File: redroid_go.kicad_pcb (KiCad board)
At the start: 2 copper layers, 70 x 95 mm, 98 parts, among them J1 USB4105-GF-A, J2 5051101892, J3 Conn_01x02_Pin, J4 Conn_01x10_Pin, Q1 UMH3N, Q2 PMOS, Q3 UMH3N, SW1 UP, SW10 A, SW11 SW_SPDT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

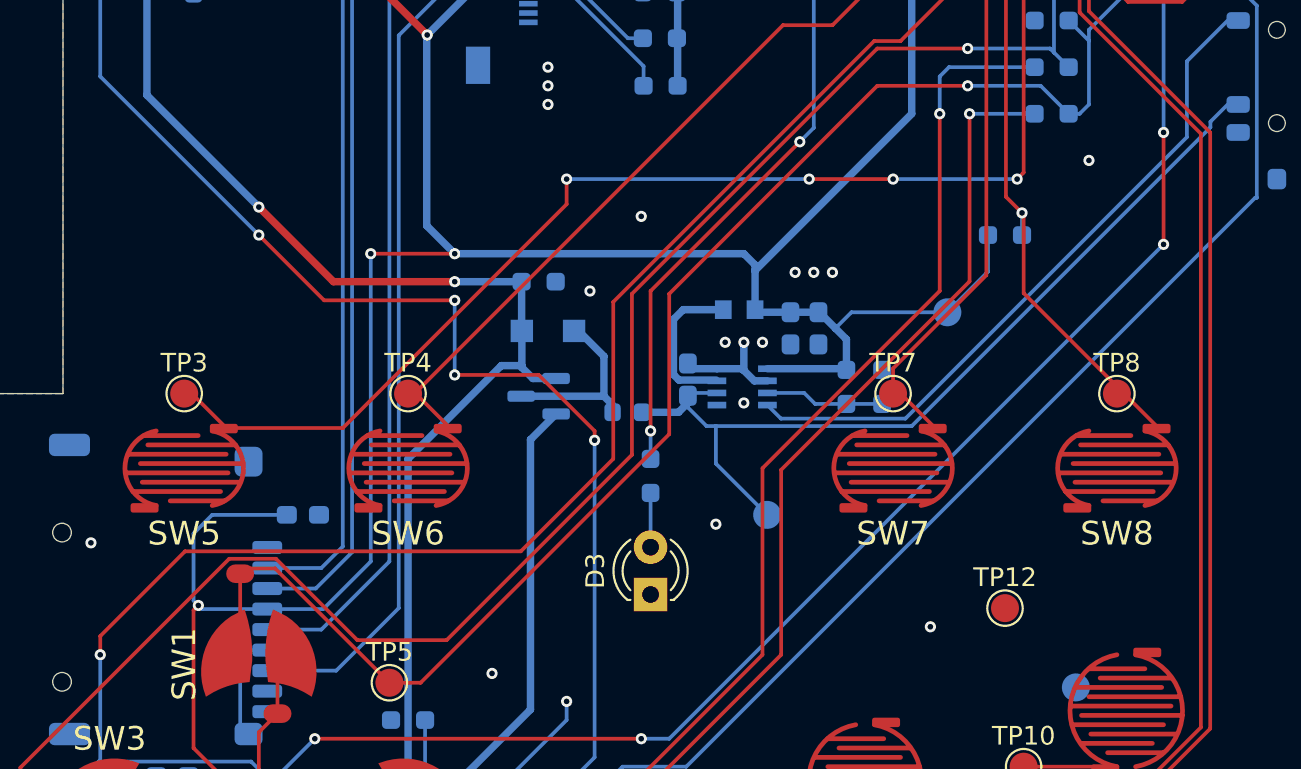
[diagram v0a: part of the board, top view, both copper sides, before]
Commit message: Update menu button footprints
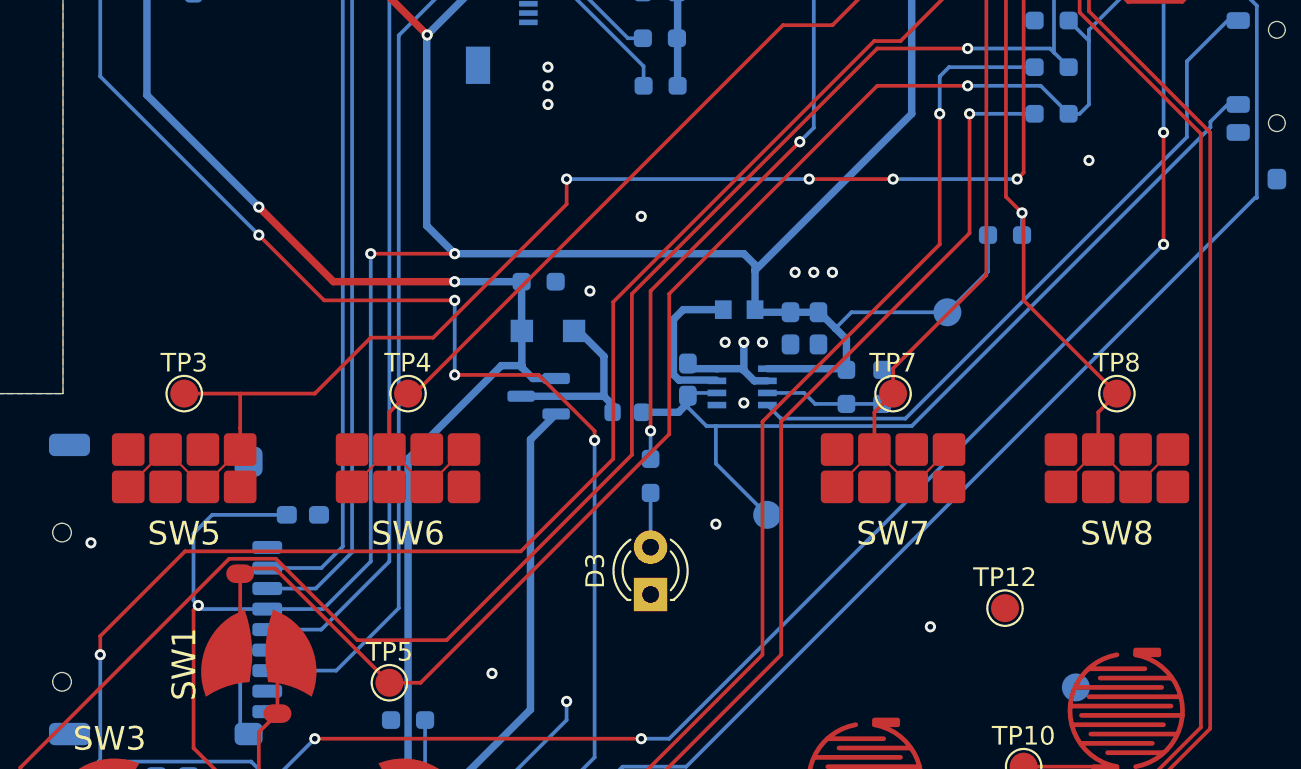
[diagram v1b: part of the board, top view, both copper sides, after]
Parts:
- SW5, SW6, SW7, SW8: footprint Conductive Button:CONDUCTIVE_BUTTON_STARTSELECT -> Conductive Button:CONDUCTIVE_BUTTON_THICK_STARTSELECT
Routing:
- net IO13: track 78.5 -> 79.8 mm
- net IO0: track 71.4 -> 72.2 mm
- net IO27: track 47.5 -> 48.3 mm
- net IO39: track 55.0 -> 55.6 mm

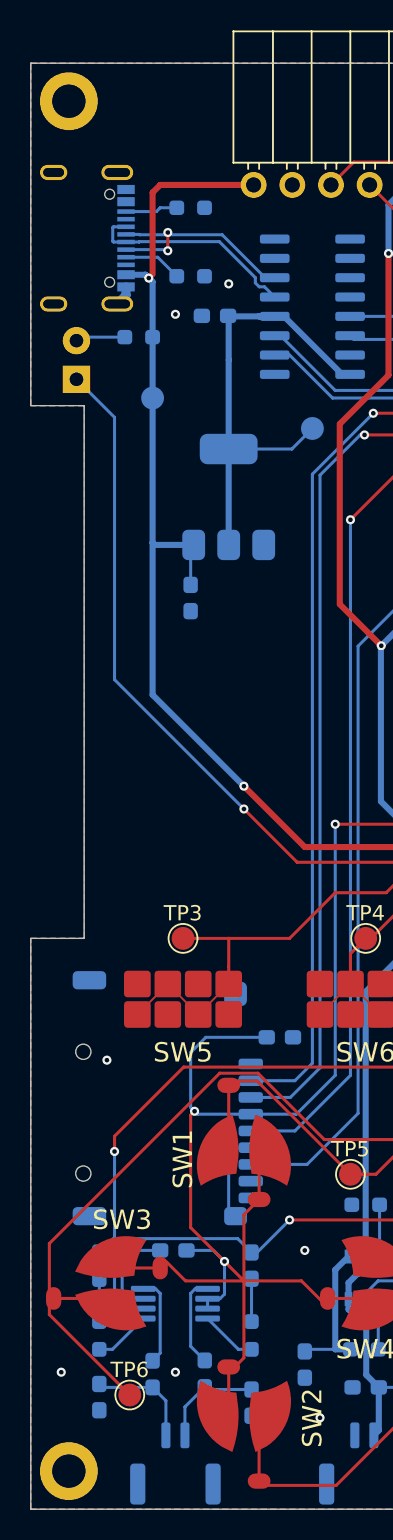
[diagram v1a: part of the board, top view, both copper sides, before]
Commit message: Fix board display margin
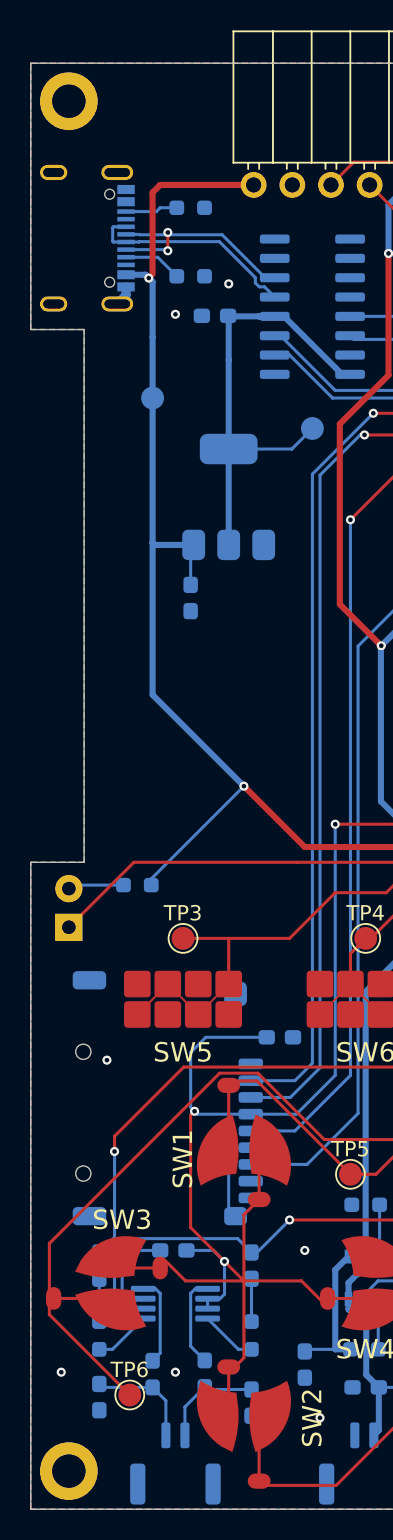
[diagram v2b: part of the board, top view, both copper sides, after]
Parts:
- moved D2 36.0 mm to (131.0, 100.3)
- moved R8 36.0 mm to (135.5, 97.5)
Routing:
- net Net-(D2-K): track 89.3 -> 68.3 mm, vias 4 -> 3
- net VBUS: track 113.9 -> 122.9 mm
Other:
- outline, holes or cut-outs redrawn
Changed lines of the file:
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@@
 	(footprint "Resistor_SMD:R_0603_1608Metric_Pad0.98x0.95mm_HandSolder"
 		(layer "B.Cu")
-		(at 135.5875 61.5 180)
+		(at 135.5 97.5 180)
 		(descr "Resistor SMD 0603 (1608 Metric), square (rectangular) end terminal, IPC_7351 nominal with elongated pad for handsoldering. (Body size source: IPC-SM-782 page 72, https://www.pcb-3d.com/wordpress/wp-content/uploads/ipc-sm-782a_amendment_1_and_2.pdf), generated with kicad-footprint-generator")
 		(tags "resistor handsolder")
@@
 	(footprint "LED_THT:LED_D3.0mm"
 		(layer "B.Cu")
-		(at 131.5 64.27 90)
+		(at 131 100.27 90)
 		(descr "LED, diameter 3.0mm, 2 pins, generated by kicad-footprint-generator")
 		(tags "LED")
@@
 	)
 	(gr_line
-		(start 128.5 101)
-		(end 132 101)
+		(start 128.5 96)
+		(end 132 96)
 		(stroke
 			(width 0.05)
@@
 	)
 	(gr_line
-		(start 128.5 66)
-		(end 132 66)
+		(start 128.5 61)
+		(end 132 61)
 		(stroke
 			(width 0.05)
@@
 	)
 	(gr_line
-		(start 132 66)
-		(end 132 101)
+		(start 132 61)
+		(end 132 96)
 		(stroke
 			(width 0.05)
-			(type default)
+			(type solid)
 		)
 		(layer "Edge.Cuts")
@@
 	(gr_line
 		(start 128.5 43.5)
-		(end 128.5 66)
+		(end 128.5 61)
 		(stroke
 			(width 0.05)
@@
 	(gr_line
 		(start 128.5 138.5)
-		(end 128.5 101)
+		(end 128.5 96)
 		(stroke
 			(width 0.05)
@@
 	)
 	(segment
+		(start 136.4125 97.5)
+		(end 136.4125 97.0875)
+		(width 0.2)
+		(layer "B.Cu")
+		(net 5)
+	)
+	(segment
+		(start 136.4125 97.0875)
+		(end 142.5 91)
+		(width 0.2)
+		(layer "B.Cu")
+		(net 5)
+	)
+	(segment
 		(start 156.5875 95)
 		(end 153 95)
@@
 	)
 	(segment
-		(start 131.73 61.5)
-		(end 131.5 61.73)
+		(start 134.5875 97.5)
+		(end 131.23 97.5)
 		(width 0.2)
 		(layer "B.Cu")
@@
 	)
 	(segment
-		(start 134.675 61.5)
-		(end 131.73 61.5)
+		(start 131.23 97.5)
+		(end 131 97.73)
 		(width 0.2)
 		(layer "B.Cu")
@@
 	)
 	(segment
-		(start 146 96)
-		(end 142.5 92.5)
+		(start 160.5 103)
+		(end 160.5 103.5)
 		(width 0.2)
 		(layer "F.Cu")
@@
 	)
 	(segment
-		(start 160.5 103)
-		(end 160.5 103.5)
+		(start 131 100.27)
+		(end 135.27 96)
 		(width 0.2)
 		(layer "F.Cu")
@@
 	)
 	(segment
+		(start 135.27 96)
+		(end 146 96)
+		(width 0.2)
+		(layer "F.Cu")
+		(net 16)
+	)
+	(segment
 		(start 153 96)
 		(end 146 96)
@@
 	)
 	(via
-		(at 142.5 92.5)
-		(size 0.6)
-		(drill 0.3)
-		(layers "F.Cu" "B.Cu")
-		(net 16)
-	)
-	(via
 		(at 153 100)
 		(size 0.6)
@@
 	)
 	(segment
-		(start 142.5 92.5)
-		(end 134 84)
-		(width 0.2)
-		(layer "B.Cu")
-		(net 16)
-	)
-	(segment
-		(start 134 66.77)
-		(end 131.5 64.27)
-		(width 0.2)
-		(layer "B.Cu")
-		(net 16)
-	)
-	(segment
 		(start 153 96)
 		(end 153 100)
@@
 	)
 	(segment
-		(start 134 84)
-		(end 134 66.77)
-		(width 0.2)
-		(layer "B.Cu")
-		(net 16)
-	)
-	(segment
 		(start 151.325 124.747629)
 		(end 151.273211 124.69584)
@@
 		(polygon
 			(pts
-				(xy 198.5 50) (xy 198.5 128.5) (xy 158.5 128.5) (xy 158.5 138.5) (xy 128.5 138.5) (xy 128.5 101)
-				(xy 132 101) (xy 132 66) (xy 128.5 66) (xy 128.5 43.5) (xy 173.5 43.5) (xy 173.5 50)
+				(xy 198.5 50) (xy 198.5 128.5) (xy 158.5 128.5) (xy 158.5 138.5) (xy 128.5 138.5) (xy 128.5 96)
+				(xy 132 96) (xy 132 61) (xy 128.5 61) (xy 128.5 43.5) (xy 173.5 43.5) (xy 173.5 50)
 			)
 		)
@@
 		(polygon
 			(pts
-				(xy 198.5 50) (xy 198.5 128.5) (xy 158.5 128.5) (xy 158.5 138.5) (xy 128.5 138.5) (xy 128.5 101)
-				(xy 132 101) (xy 132 66) (xy 128.5 66) (xy 128.5 43.5) (xy 173.5 43.5) (xy 173.5 50)
+				(xy 198.5 50) (xy 198.5 128.5) (xy 158.5 128.5) (xy 158.5 138.5) (xy 128.5 138.5) (xy 128.5 96)
+				(xy 132 96) (xy 132 61) (xy 128.5 61) (xy 128.5 43.5) (xy 173.5 43.5) (xy 173.5 50)
 			)
 		)

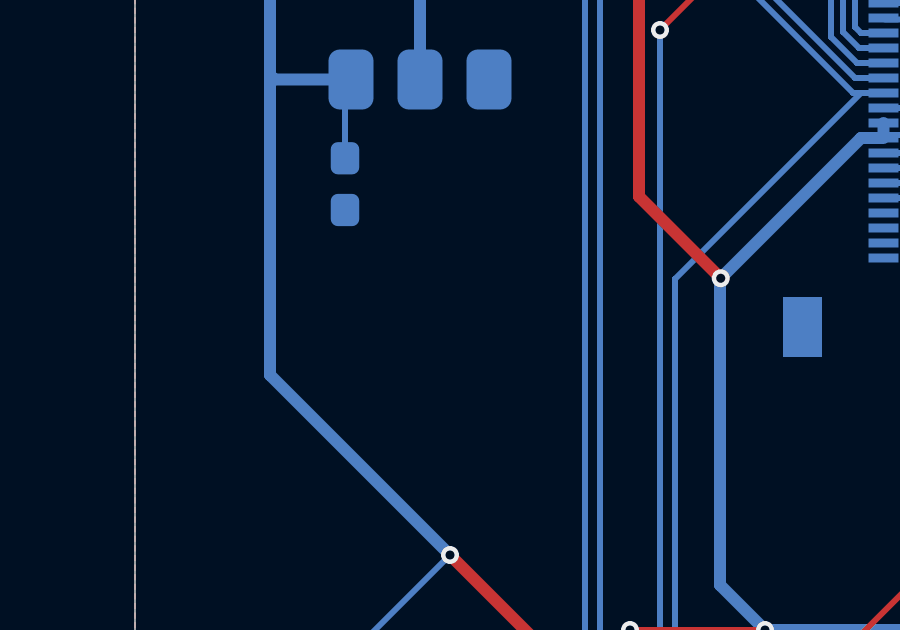
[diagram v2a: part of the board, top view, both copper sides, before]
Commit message: Add missing via
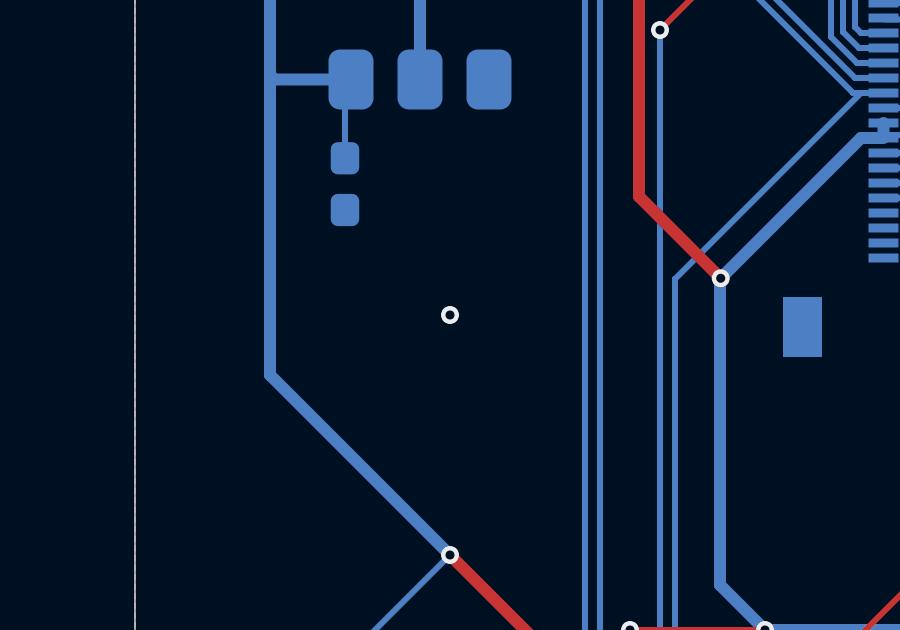
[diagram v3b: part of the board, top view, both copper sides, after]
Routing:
- net GND: vias 34 -> 35
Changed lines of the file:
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@@
+	)
+	(via
+		(at 142.5 83)
+		(size 0.6)
+		(drill 0.3)
+		(layers "F.Cu" "B.Cu")
+		(free yes)
+		(net 1)
 	)
 	(via

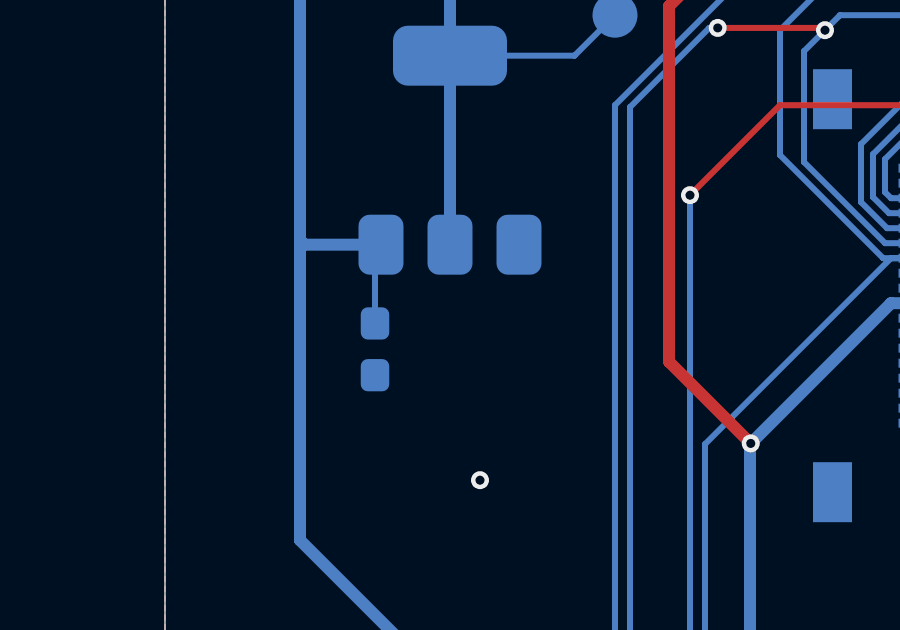
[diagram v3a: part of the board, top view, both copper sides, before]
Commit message: Fix 3V3_SERIAL capacitors
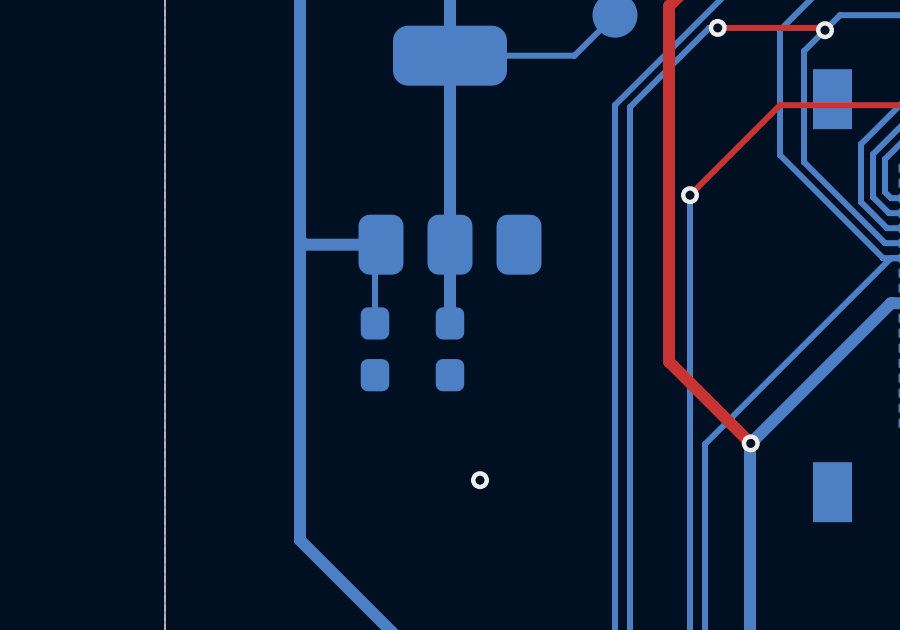
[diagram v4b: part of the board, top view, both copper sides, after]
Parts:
- added C18: 22uF, Capacitor_SMD:C_0603_1608Metric_Pad1.08x0.95mm_HandSolder, B.Cu at (141.5, 78.6)
- C14, C15: value 0.1uF -> 220pF
- C17: value 0.1uF -> 10uF
- R6: value 100k -> 2k
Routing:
- net P3V3_SERIAL: track 33.0 -> 35.6 mm
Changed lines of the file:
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@@
 			(layers "F.Cu" "F.Mask")
 			(roundrect_rratio 0.125)
-			(pinfunction "P$ACTIVE")
-			(pintype "bidirectional")
 			(solder_mask_margin 0.1016)
 			(solder_paste_margin 0)
@@
 			(layers "F.Cu" "F.Mask")
 			(roundrect_rratio 0.125)
-			(pinfunction "P$ACTIVE")
-			(pintype "bidirectional")
 			(solder_mask_margin 0.1016)
 			(solder_paste_margin 0)
@@
 			(layers "F.Cu" "F.Mask")
 			(roundrect_rratio 0.125)
-			(pinfunction "P$ACTIVE")
-			(pintype "bidirectional")
 			(solder_mask_margin 0.1016)
 			(solder_paste_margin 0)
@@
 			)
 		)
-		(property "Value" "0.1uF"
+		(property "Value" "10uF"
 			(at 0 -1.43 90)
 			(layer "B.Fab")
@@
 			)
 		)
-		(property "Value" "0.1uF"
+		(property "Value" "220pF"
 			(at 0 -1.43 90)
 			(layer "B.Fab")
@@
 		)
 	)
+	(footprint "Capacitor_SMD:C_0603_1608Metric_Pad1.08x0.95mm_HandSolder"
+		(layer "B.Cu")
+		(at 141.5 78.6375 -90)
+		(descr "Capacitor SMD 0603 (1608 Metric), square (rectangular) end terminal, IPC_7351 nominal with elongated pad for handsoldering. (Body size source: IPC-SM-782 page 76, https://www.pcb-3d.com/wordpress/wp-content/uploads/ipc-sm-782a_amendment_1_and_2.pdf), generated with kicad-footprint-generator")
+		(tags "capacitor handsolder")
+		(property "Reference" "C18"
+			(at 0 -2 90)
+			(layer "B.SilkS")
+			(effects
+				(font
+					(size 1 1)
+					(thickness 0.15)
+				)
+				(justify mirror)
+			)
+		)
+		(property "Value" "22uF"
+			(at 0 -1.43 90)
+			(layer "B.Fab")
+			(effects
+				(font
+					(size 1 1)
+					(thickness 0.15)
+				)
+				(justify mirror)
+			)
+		)
+		(property "Datasheet" ""
+			(at 0 0 90)
+			(unlocked yes)
+			(layer "B.Fab")
+			(hide yes)
+			(effects
+				(font
+					(size 1.27 1.27)
+					(thickness 0.15)
+				)
+				(justify mirror)
+			)
+		)
+		(property "Description" "Unpolarized capacitor"
+			(at 0 0 90)
+			(unlocked yes)
+			(layer "B.Fab")
+			(hide yes)
+			(effects
+				(font
+					(size 1.27 1.27)
+					(thickness 0.15)
+				)
+				(justify mirror)
+			)
+		)
+		(property ki_fp_filters "C_*")
+		(sheetname "/")
+		(sheetfile "redroid_go.kicad_sch")
+		(attr smd)
+		(fp_line
+			(start -0.146267 0.51)
+			(end 0.146267 0.51)
+			(stroke
+				(width 0.12)
+				(type solid)
+			)
+			(layer "B.SilkS")
+		)
+		(fp_line
+			(start -0.146267 -0.51)
+			(end 0.146267 -0.51)
+			(stroke
+				(width 0.12)
+				(type solid)
+			)
+			(layer "B.SilkS")
+		)
+		(fp_line
+			(start -1.65 0.73)
+			(end 1.65 0.73)
+			(stroke
+				(width 0.05)
+				(type solid)
+			)
+			(layer "B.CrtYd")
+		)
+		(fp_line
+			(start 1.65 0.73)
+			(end 1.65 -0.73)
+			(stroke
+				(width 0.05)
+				(type solid)
+			)
+			(layer "B.CrtYd")
+		)
+		(fp_line
+			(start -1.65 -0.73)
+			(end -1.65 0.73)
+			(stroke
+				(width 0.05)
+				(type solid)
+			)
+			(layer "B.CrtYd")
+		)
+		(fp_line
+			(start 1.65 -0.73)
+			(end -1.65 -0.73)
+			(stroke
+				(width 0.05)
+				(type solid)
+			)
+			(layer "B.CrtYd")
+		)
+		(fp_line
+			(start -0.8 0.4)
+			(end 0.8 0.4)
+			(stroke
+				(width 0.1)
+				(type solid)
+			)
+			(layer "B.Fab")
+		)
+		(fp_line
+			(start 0.8 0.4)
+			(end 0.8 -0.4)
+			(stroke
+				(width 0.1)
+				(type solid)
+			)
+			(layer "B.Fab")
+		)
+		(fp_line
+			(start -0.8 -0.4)
+			(end -0.8 0.4)
+			(stroke
+				(width 0.1)
+				(type solid)
+			)
+			(layer "B.Fab")
+		)
+		(fp_line
+			(start 0.8 -0.4)
+			(end -0.8 -0.4)
+			(stroke
+				(width 0.1)
+				(type solid)
+			)
+			(layer "B.Fab")
+		)
+		(fp_text user "${REFERENCE}"
+			(at 0 0 90)
+			(layer "B.Fab")
+			(effects
+				(font
+					(size 0.4 0.4)
+					(thickness 0.06)
+				)
+				(justify mirror)
+			)
+		)
+		(pad "1" smd roundrect
+			(at -0.8625 0 270)
+			(size 1.075 0.95)
+			(layers "B.Cu" "B.Mask" "B.Paste")
+			(roundrect_rratio 0.25)
+			(net 112 "P3V3_SERIAL")
+			(pintype "passive")
+		)
+		(pad "2" smd roundrect
+			(at 0.8625 0 270)
+			(size 1.075 0.95)
+			(layers "B.Cu" "B.Mask" "B.Paste")
+			(roundrect_rratio 0.25)
+			(net 1 "GND")
+			(pintype "passive")
+		)
+		(embedded_fonts no)
+		(model "${KICAD9_3DMODEL_DIR}/Capacitor_SMD.3dshapes/C_0603_1608Metric.wrl"
+			(offset
+				(xyz 0 0 0)
+			)
+			(scale
+				(xyz 1 1 1)
+			)
+			(rotate
+				(xyz 0 0 0)
+			)
+		)
+	)
 	(footprint "Inductor_SMD:L_Murata_LQH2MCNxxxx02_2.0x1.6mm"
 		(layer "B.Cu")
@@
 			)
 		)
-		(property "Value" "100k"
+		(property "Value" "2k"
 			(at 0 -1.43 0)
 			(layer "B.Fab")
@@
 			)
 		)
-		(property "Value" "0.1uF"
+		(property "Value" "220pF"
 			(at 0 -1.43 90)
 			(layer "B.Fab")
@@
 		(tags "5051101892 ")
 		(property "Reference" "J2"
-			(at 0 0 270)
+			(at -9.65 0 0)
 			(unlocked yes)
 			(layer "B.SilkS")
@@
 	)
 	(segment
+		(start 151.3625 133.325)
+		(end 151.0375 133.65)
+		(width 0.4)
+		(layer "B.Cu")
+		(net 2)
+	)
+	(segment
+		(start 151.3625 130.5)
+		(end 151.3625 133.325)
+		(width 0.4)
+		(layer "B.Cu")
+		(net 2)
+	)
+	(segment
 		(start 155.9125 134.5)
 		(end 155.9125 131.825)
@@
 	)
 	(segment
-		(start 151.3625 130.5)
-		(end 151.3625 133.325)
-		(width 0.4)
-		(layer "B.Cu")
-		(net 2)
-	)
-	(segment
 		(start 152 123)
 		(end 150 123)
@@
 	)
 	(segment
-		(start 151.3625 133.325)
-		(end 151.0375 133.65)
-		(width 0.4)
-		(layer "B.Cu")
-		(net 2)
-	)
-	(segment
 		(start 158.4375 102.090449)
 		(end 157.0625 103.465449)
@@
 		(width 0.4)
 		(layer "B.Cu")
+		(net 112)
+	)
+	(segment
+		(start 141.5 75.15)
+		(end 141.5 77.775)
+		(width 0.4)
+		(layer "B.Cu")
